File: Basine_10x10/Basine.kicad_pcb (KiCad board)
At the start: 2 copper layers, 100 x 100 mm, 55 parts, among them J1 2060-451/998-404, J10 2060-451/998-404, J11 2060-451/998-404, J12 2060-451/998-404, J13 2060-451/998-404, J14 2060-451/998-404, J15 2060-451/998-404, J16 2060-451/998-404, J17 2060-451/998-404, J18 2060-451/998-404, J2 2060-451/998-404, J3 2060-451/998-404, J4 2060-451/998-404, J5 2060-451/998-404, J6 2060-451/998-404, J7 2060-451/998-404, J8 2060-451/998-404, J9 2060-451/998-404

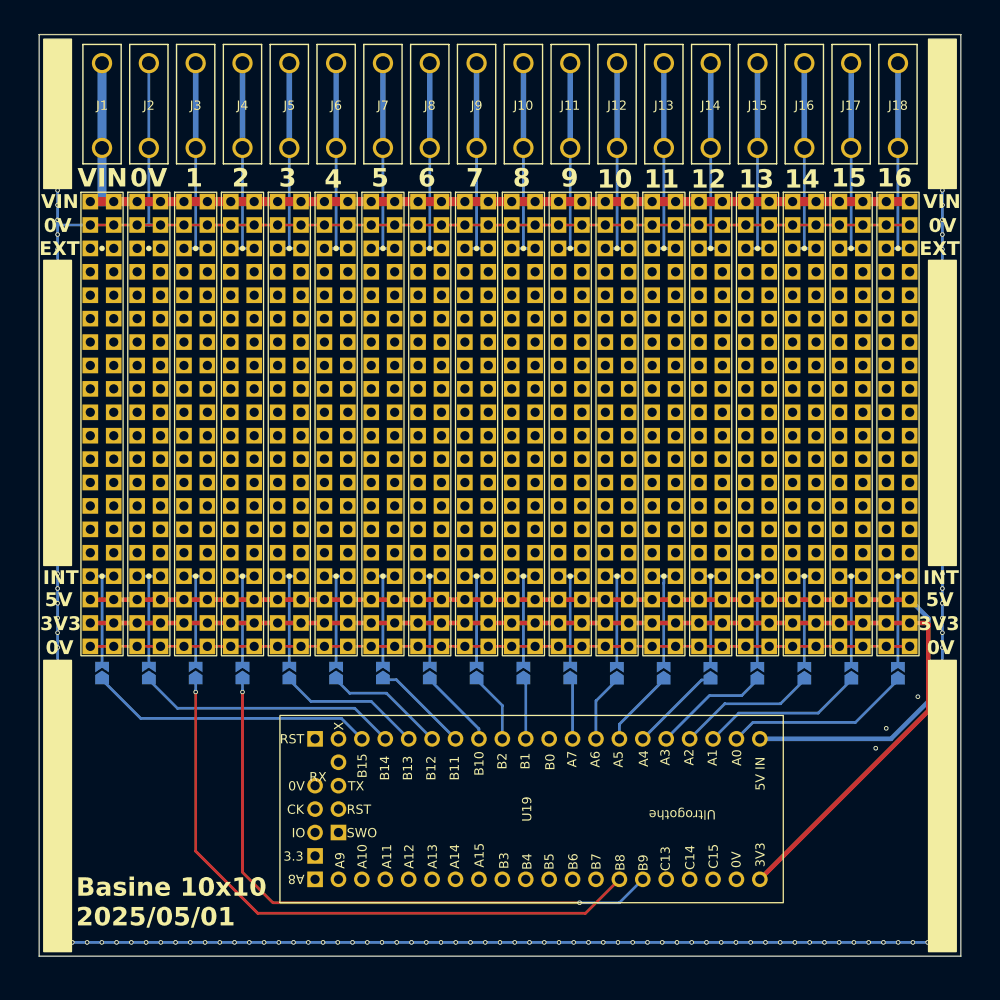
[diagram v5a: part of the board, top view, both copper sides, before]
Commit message: Basine_10x10 : moins de vias
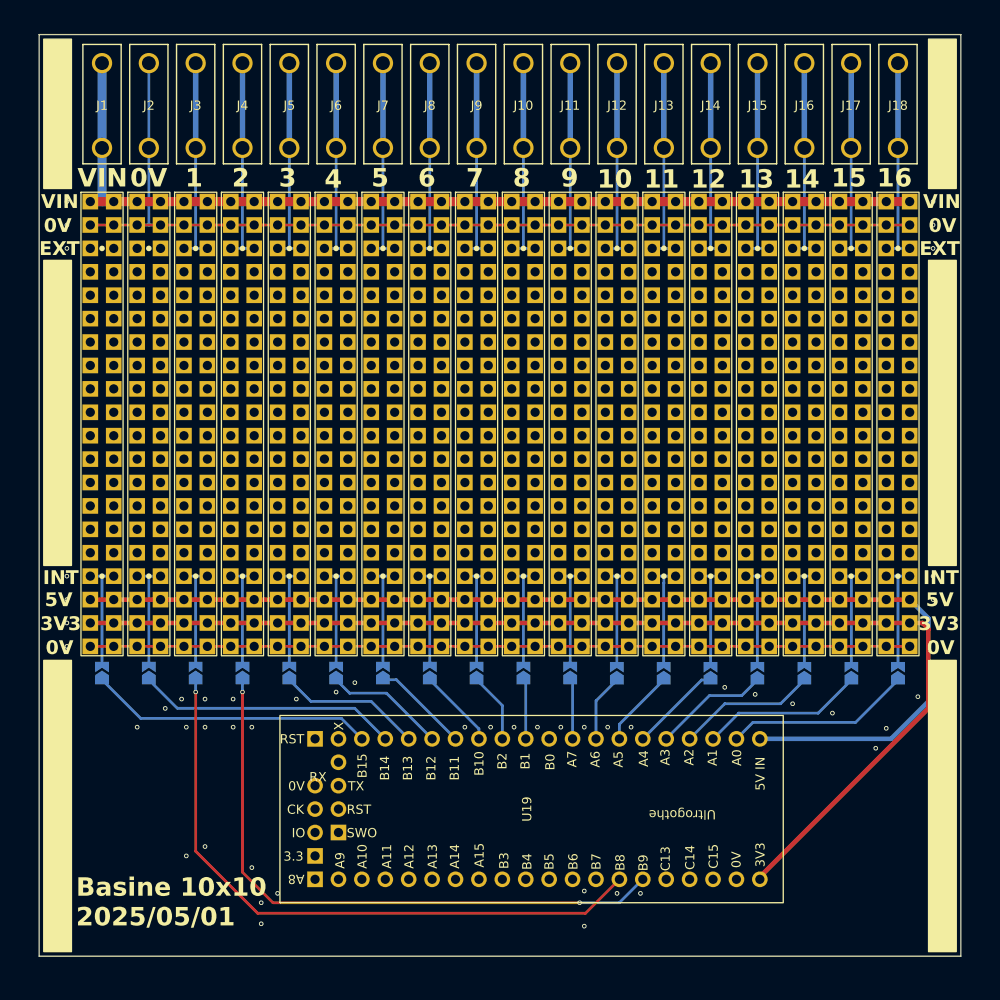
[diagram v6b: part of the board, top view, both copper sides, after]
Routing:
- net 0V: track 489.5 -> 197.9 mm, vias 184 -> 109

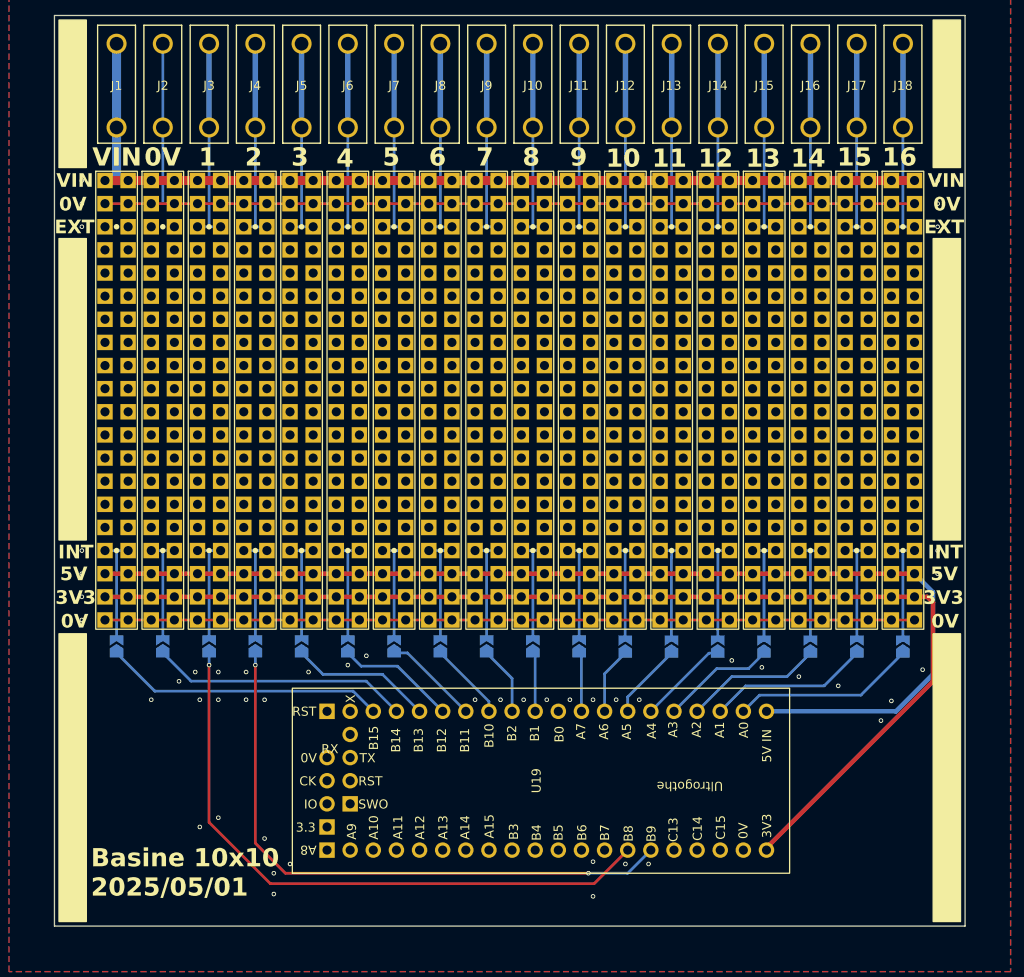
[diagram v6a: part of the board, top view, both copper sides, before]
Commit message: Basine 10x10: modification ultrogothe, allumettes, 3v3 en option
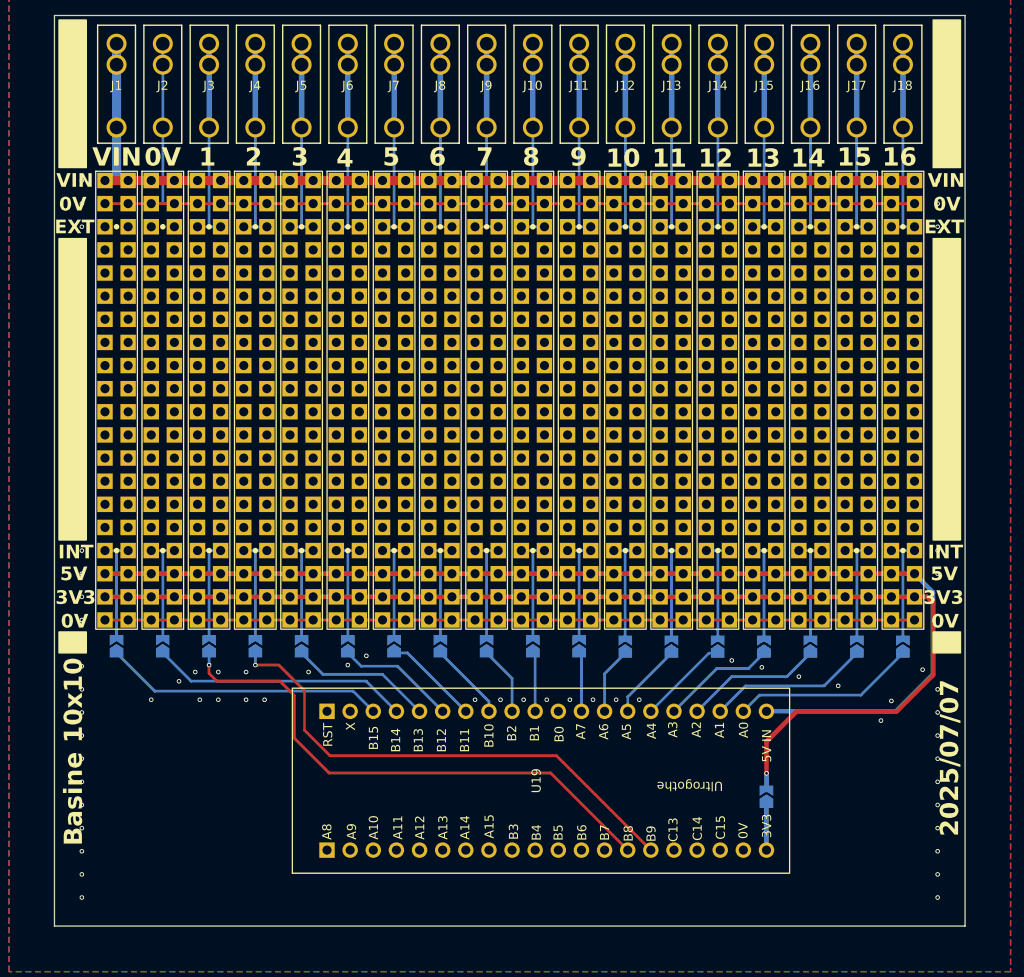
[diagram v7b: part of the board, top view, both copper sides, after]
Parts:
- added JP19: SolderJumper_2_Open, Jumper:SolderJumper-2_P1.3mm_Open_TrianglePad1.0x1.5mm, B.Cu at (178.2, 185.8)
- J1, J10, J11, J12, J13, J14, J15, J16, J17, J18, J2, J3, J4, J5, J6, J7, J8, J9: footprint Chimere_comps:CONN_2060-1451_998-404_WAGO -> Chimere_comps:Conn_bornier_et_wago
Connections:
- U1 pad 10: (no net) -> unconnected-(U1-Pad10)
- U1 pad 11: (no net) -> unconnected-(U1-Pad11)
- U1 pad 12: (no net) -> unconnected-(U1-Pad12)
- U1 pad 13: (no net) -> unconnected-(U1-Pad13)_1
- U1 pad 14: (no net) -> unconnected-(U1-Pad14)
- U1 pad 15: (no net) -> unconnected-(U1-Pad15)
- U1 pad 16: (no net) -> unconnected-(U1-Pad16)
- U1 pad 17: (no net) -> unconnected-(U1-Pad17)
- U1 pad 5: (no net) -> unconnected-(U1-Pad5)
- U1 pad 6: (no net) -> unconnected-(U1-Pad6)
- U1 pad 7: (no net) -> unconnected-(U1-Pad7)_1
- U1 pad 8: (no net) -> unconnected-(U1-Pad8)_1
- U1 pad 9: (no net) -> unconnected-(U1-Pad9)
- U10 pad 10: (no net) -> unconnected-(U10-Pad10)
- U10 pad 11: (no net) -> unconnected-(U10-Pad11)
- U10 pad 12: (no net) -> unconnected-(U10-Pad12)_1
- U10 pad 13: (no net) -> unconnected-(U10-Pad13)
- U10 pad 14: (no net) -> unconnected-(U10-Pad14)_1
- U10 pad 15: (no net) -> unconnected-(U10-Pad15)
- U10 pad 16: (no net) -> unconnected-(U10-Pad16)
- U10 pad 17: (no net) -> unconnected-(U10-Pad17)_1
- U10 pad 5: (no net) -> unconnected-(U10-Pad5)_1
- U10 pad 6: (no net) -> unconnected-(U10-Pad6)
- U10 pad 7: (no net) -> unconnected-(U10-Pad7)
- U10 pad 8: (no net) -> unconnected-(U10-Pad8)
- U10 pad 9: (no net) -> unconnected-(U10-Pad9)
- U11 pad 10: (no net) -> unconnected-(U11-Pad10)
- U11 pad 11: (no net) -> unconnected-(U11-Pad11)
- U11 pad 12: (no net) -> unconnected-(U11-Pad12)_1
- U11 pad 13: (no net) -> unconnected-(U11-Pad13)_1
- U11 pad 14: (no net) -> unconnected-(U11-Pad14)_1
- U11 pad 15: (no net) -> unconnected-(U11-Pad15)
- U11 pad 16: (no net) -> unconnected-(U11-Pad16)_1
- U11 pad 17: (no net) -> unconnected-(U11-Pad17)_1
- U11 pad 5: (no net) -> unconnected-(U11-Pad5)_1
- U11 pad 6: (no net) -> unconnected-(U11-Pad6)
- U11 pad 7: (no net) -> unconnected-(U11-Pad7)
- U11 pad 8: (no net) -> unconnected-(U11-Pad8)_1
- U11 pad 9: (no net) -> unconnected-(U11-Pad9)
- U12 pad 10: (no net) -> unconnected-(U12-Pad10)_1
- U12 pad 11: (no net) -> unconnected-(U12-Pad11)_1
- U12 pad 12: (no net) -> unconnected-(U12-Pad12)
- U12 pad 13: (no net) -> unconnected-(U12-Pad13)_1
- U12 pad 14: (no net) -> unconnected-(U12-Pad14)
- U12 pad 15: (no net) -> unconnected-(U12-Pad15)_1
- U12 pad 16: (no net) -> unconnected-(U12-Pad16)
- U12 pad 17: (no net) -> unconnected-(U12-Pad17)_1
- U12 pad 5: (no net) -> unconnected-(U12-Pad5)_1
- U12 pad 6: (no net) -> unconnected-(U12-Pad6)_1
- U12 pad 7: (no net) -> unconnected-(U12-Pad7)
- U12 pad 8: (no net) -> unconnected-(U12-Pad8)
- U12 pad 9: (no net) -> unconnected-(U12-Pad9)_1
- U13 pad 10: (no net) -> unconnected-(U13-Pad10)
- U13 pad 11: (no net) -> unconnected-(U13-Pad11)
- U13 pad 12: (no net) -> unconnected-(U13-Pad12)
- U13 pad 13: (no net) -> unconnected-(U13-Pad13)
- U13 pad 14: (no net) -> unconnected-(U13-Pad14)
- U13 pad 15: (no net) -> unconnected-(U13-Pad15)_1
- U13 pad 16: (no net) -> unconnected-(U13-Pad16)
- U13 pad 17: (no net) -> unconnected-(U13-Pad17)_1
- U13 pad 5: (no net) -> unconnected-(U13-Pad5)_1
- U13 pad 6: (no net) -> unconnected-(U13-Pad6)
- U13 pad 7: (no net) -> unconnected-(U13-Pad7)_1
- U13 pad 8: (no net) -> unconnected-(U13-Pad8)
- U13 pad 9: (no net) -> unconnected-(U13-Pad9)_1
- U14 pad 10: (no net) -> unconnected-(U14-Pad10)
- U14 pad 11: (no net) -> unconnected-(U14-Pad11)
- U14 pad 12: (no net) -> unconnected-(U14-Pad12)
- U14 pad 13: (no net) -> unconnected-(U14-Pad13)_1
- U14 pad 14: (no net) -> unconnected-(U14-Pad14)_1
- U14 pad 15: (no net) -> unconnected-(U14-Pad15)
- U14 pad 16: (no net) -> unconnected-(U14-Pad16)_1
- U14 pad 17: (no net) -> unconnected-(U14-Pad17)
- U14 pad 5: (no net) -> unconnected-(U14-Pad5)
- U14 pad 6: (no net) -> unconnected-(U14-Pad6)_1
- U14 pad 7: (no net) -> unconnected-(U14-Pad7)
- U14 pad 8: (no net) -> unconnected-(U14-Pad8)
- U14 pad 9: (no net) -> unconnected-(U14-Pad9)_1
- U15 pad 10: (no net) -> unconnected-(U15-Pad10)_1
- U15 pad 11: (no net) -> unconnected-(U15-Pad11)_1
- U15 pad 12: (no net) -> unconnected-(U15-Pad12)
- U15 pad 13: (no net) -> unconnected-(U15-Pad13)_1
- U15 pad 14: (no net) -> unconnected-(U15-Pad14)
- U15 pad 15: (no net) -> unconnected-(U15-Pad15)
- U15 pad 16: (no net) -> unconnected-(U15-Pad16)
- U15 pad 17: (no net) -> unconnected-(U15-Pad17)_1
- U15 pad 5: (no net) -> unconnected-(U15-Pad5)_1
- U15 pad 6: (no net) -> unconnected-(U15-Pad6)_1
- U15 pad 7: (no net) -> unconnected-(U15-Pad7)
- U15 pad 8: (no net) -> unconnected-(U15-Pad8)_1
- U15 pad 9: (no net) -> unconnected-(U15-Pad9)_1
- U16 pad 10: (no net) -> unconnected-(U16-Pad10)_1
- U16 pad 11: (no net) -> unconnected-(U16-Pad11)_1
- U16 pad 12: (no net) -> unconnected-(U16-Pad12)
- U16 pad 13: (no net) -> unconnected-(U16-Pad13)
- U16 pad 14: (no net) -> unconnected-(U16-Pad14)
- U16 pad 15: (no net) -> unconnected-(U16-Pad15)_1
- U16 pad 16: (no net) -> unconnected-(U16-Pad16)
- U16 pad 17: (no net) -> unconnected-(U16-Pad17)
- U16 pad 5: (no net) -> unconnected-(U16-Pad5)
- U16 pad 6: (no net) -> unconnected-(U16-Pad6)
- U16 pad 7: (no net) -> unconnected-(U16-Pad7)
- U16 pad 8: (no net) -> unconnected-(U16-Pad8)_1
- U16 pad 9: (no net) -> unconnected-(U16-Pad9)_1
- U17 pad 10: (no net) -> unconnected-(U17-Pad10)_1
- U17 pad 11: (no net) -> unconnected-(U17-Pad11)_1
- U17 pad 12: (no net) -> unconnected-(U17-Pad12)_1
- U17 pad 13: (no net) -> unconnected-(U17-Pad13)
- U17 pad 14: (no net) -> unconnected-(U17-Pad14)_1
- U17 pad 15: (no net) -> unconnected-(U17-Pad15)_1
- U17 pad 16: (no net) -> unconnected-(U17-Pad16)
- U17 pad 17: (no net) -> unconnected-(U17-Pad17)_1
- U17 pad 5: (no net) -> unconnected-(U17-Pad5)
- U17 pad 6: (no net) -> unconnected-(U17-Pad6)_1
- U17 pad 7: (no net) -> unconnected-(U17-Pad7)_1
- U17 pad 8: (no net) -> unconnected-(U17-Pad8)
- U17 pad 9: (no net) -> unconnected-(U17-Pad9)_1
- U18 pad 10: (no net) -> unconnected-(U18-Pad10)
- U18 pad 11: (no net) -> unconnected-(U18-Pad11)
- U18 pad 12: (no net) -> unconnected-(U18-Pad12)_1
- U18 pad 13: (no net) -> unconnected-(U18-Pad13)
- U18 pad 14: (no net) -> unconnected-(U18-Pad14)_1
- U18 pad 15: (no net) -> unconnected-(U18-Pad15)
- U18 pad 16: (no net) -> unconnected-(U18-Pad16)_1
- U18 pad 17: (no net) -> unconnected-(U18-Pad17)
- U18 pad 5: (no net) -> unconnected-(U18-Pad5)
- U18 pad 6: (no net) -> unconnected-(U18-Pad6)_1
- U18 pad 7: (no net) -> unconnected-(U18-Pad7)_1
- U18 pad 8: (no net) -> unconnected-(U18-Pad8)_1
- U18 pad 9: (no net) -> unconnected-(U18-Pad9)_1
- U19 pad 20: 3V3 -> Net-(JP19-A)
- U2 pad 10: (no net) -> unconnected-(U2-Pad10)
- U2 pad 11: (no net) -> unconnected-(U2-Pad11)_1
- U2 pad 12: (no net) -> unconnected-(U2-Pad12)
- U2 pad 13: (no net) -> unconnected-(U2-Pad13)
- U2 pad 14: (no net) -> unconnected-(U2-Pad14)_1
- U2 pad 15: (no net) -> unconnected-(U2-Pad15)
- U2 pad 16: (no net) -> unconnected-(U2-Pad16)
- U2 pad 17: (no net) -> unconnected-(U2-Pad17)
- U2 pad 5: (no net) -> unconnected-(U2-Pad5)
- U2 pad 6: (no net) -> unconnected-(U2-Pad6)
- U2 pad 7: (no net) -> unconnected-(U2-Pad7)_1
- U2 pad 8: (no net) -> unconnected-(U2-Pad8)_1
- U2 pad 9: (no net) -> unconnected-(U2-Pad9)_1
- U3 pad 10: (no net) -> unconnected-(U3-Pad10)_1
- U3 pad 11: (no net) -> unconnected-(U3-Pad11)
- U3 pad 12: (no net) -> unconnected-(U3-Pad12)_1
- U3 pad 13: (no net) -> unconnected-(U3-Pad13)_1
- U3 pad 14: (no net) -> unconnected-(U3-Pad14)
- U3 pad 15: (no net) -> unconnected-(U3-Pad15)
- U3 pad 16: (no net) -> unconnected-(U3-Pad16)_1
- U3 pad 17: (no net) -> unconnected-(U3-Pad17)
- U3 pad 5: (no net) -> unconnected-(U3-Pad5)_1
- U3 pad 6: (no net) -> unconnected-(U3-Pad6)_1
- U3 pad 7: (no net) -> unconnected-(U3-Pad7)_1
- U3 pad 8: (no net) -> unconnected-(U3-Pad8)
- U3 pad 9: (no net) -> unconnected-(U3-Pad9)_1
- U4 pad 10: (no net) -> unconnected-(U4-Pad10)
- U4 pad 11: (no net) -> unconnected-(U4-Pad11)
- U4 pad 12: (no net) -> unconnected-(U4-Pad12)_1
- U4 pad 13: (no net) -> unconnected-(U4-Pad13)
- U4 pad 14: (no net) -> unconnected-(U4-Pad14)_1
- U4 pad 15: (no net) -> unconnected-(U4-Pad15)_1
- U4 pad 16: (no net) -> unconnected-(U4-Pad16)_1
- U4 pad 17: (no net) -> unconnected-(U4-Pad17)
- U4 pad 5: (no net) -> unconnected-(U4-Pad5)_1
- U4 pad 6: (no net) -> unconnected-(U4-Pad6)_1
- U4 pad 7: (no net) -> unconnected-(U4-Pad7)
- U4 pad 8: (no net) -> unconnected-(U4-Pad8)_1
- U4 pad 9: (no net) -> unconnected-(U4-Pad9)_1
- U5 pad 10: (no net) -> unconnected-(U5-Pad10)_1
- U5 pad 11: (no net) -> unconnected-(U5-Pad11)
- U5 pad 12: (no net) -> unconnected-(U5-Pad12)
- U5 pad 13: (no net) -> unconnected-(U5-Pad13)_1
- U5 pad 14: (no net) -> unconnected-(U5-Pad14)_1
- U5 pad 15: (no net) -> unconnected-(U5-Pad15)_1
- U5 pad 16: (no net) -> unconnected-(U5-Pad16)_1
- U5 pad 17: (no net) -> unconnected-(U5-Pad17)
- U5 pad 5: (no net) -> unconnected-(U5-Pad5)_1
- U5 pad 6: (no net) -> unconnected-(U5-Pad6)
- U5 pad 7: (no net) -> unconnected-(U5-Pad7)_1
- U5 pad 8: (no net) -> unconnected-(U5-Pad8)
- U5 pad 9: (no net) -> unconnected-(U5-Pad9)
- U6 pad 10: (no net) -> unconnected-(U6-Pad10)_1
- U6 pad 11: (no net) -> unconnected-(U6-Pad11)_1
- U6 pad 12: (no net) -> unconnected-(U6-Pad12)
- U6 pad 13: (no net) -> unconnected-(U6-Pad13)_1
- U6 pad 14: (no net) -> unconnected-(U6-Pad14)_1
- U6 pad 15: (no net) -> unconnected-(U6-Pad15)
- U6 pad 16: (no net) -> unconnected-(U6-Pad16)_1
- U6 pad 17: (no net) -> unconnected-(U6-Pad17)_1
- U6 pad 5: (no net) -> unconnected-(U6-Pad5)_1
- U6 pad 6: (no net) -> unconnected-(U6-Pad6)_1
- U6 pad 7: (no net) -> unconnected-(U6-Pad7)_1
- U6 pad 8: (no net) -> unconnected-(U6-Pad8)_1
- U6 pad 9: (no net) -> unconnected-(U6-Pad9)_1
- U7 pad 10: (no net) -> unconnected-(U7-Pad10)
- U7 pad 11: (no net) -> unconnected-(U7-Pad11)_1
- U7 pad 12: (no net) -> unconnected-(U7-Pad12)_1
- U7 pad 13: (no net) -> unconnected-(U7-Pad13)
- U7 pad 14: (no net) -> unconnected-(U7-Pad14)
- U7 pad 15: (no net) -> unconnected-(U7-Pad15)
- U7 pad 16: (no net) -> unconnected-(U7-Pad16)_1
- U7 pad 17: (no net) -> unconnected-(U7-Pad17)
- U7 pad 5: (no net) -> unconnected-(U7-Pad5)
- U7 pad 6: (no net) -> unconnected-(U7-Pad6)_1
- U7 pad 7: (no net) -> unconnected-(U7-Pad7)_1
- U7 pad 8: (no net) -> unconnected-(U7-Pad8)_1
- U7 pad 9: (no net) -> unconnected-(U7-Pad9)_1
- U8 pad 10: (no net) -> unconnected-(U8-Pad10)_1
- U8 pad 11: (no net) -> unconnected-(U8-Pad11)
- U8 pad 12: (no net) -> unconnected-(U8-Pad12)_1
- U8 pad 13: (no net) -> unconnected-(U8-Pad13)_1
- U8 pad 14: (no net) -> unconnected-(U8-Pad14)
- U8 pad 15: (no net) -> unconnected-(U8-Pad15)
- U8 pad 16: (no net) -> unconnected-(U8-Pad16)_1
- U8 pad 17: (no net) -> unconnected-(U8-Pad17)_1
- U8 pad 5: (no net) -> unconnected-(U8-Pad5)
- U8 pad 6: (no net) -> unconnected-(U8-Pad6)_1
- U8 pad 7: (no net) -> unconnected-(U8-Pad7)
- U8 pad 8: (no net) -> unconnected-(U8-Pad8)
- U8 pad 9: (no net) -> unconnected-(U8-Pad9)_1
- U9 pad 10: (no net) -> unconnected-(U9-Pad10)_1
- U9 pad 11: (no net) -> unconnected-(U9-Pad11)_1
- U9 pad 12: (no net) -> unconnected-(U9-Pad12)_1
- U9 pad 13: (no net) -> unconnected-(U9-Pad13)
- U9 pad 14: (no net) -> unconnected-(U9-Pad14)
- U9 pad 15: (no net) -> unconnected-(U9-Pad15)
- U9 pad 16: (no net) -> unconnected-(U9-Pad16)
- U9 pad 17: (no net) -> unconnected-(U9-Pad17)_1
- U9 pad 5: (no net) -> unconnected-(U9-Pad5)
- U9 pad 6: (no net) -> unconnected-(U9-Pad6)
- U9 pad 7: (no net) -> unconnected-(U9-Pad7)
- U9 pad 8: (no net) -> unconnected-(U9-Pad8)
- U9 pad 9: (no net) -> unconnected-(U9-Pad9)_1
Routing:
- net CAN_TX: track 66.7 -> 55.7 mm, vias 2 -> 1
- net CAN_RX: track 68.9 -> 59.0 mm
- net Net-(JP19-A): track 0.00 -> 5.14 mm
- net 3V3: track 125.9 -> 125.8 mm, vias 0 -> 1
- net 0V: vias 109 -> 99
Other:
- board text added: "2025/07/07"
- board text added: "Basine 10x10"
- board text removed: "Basine 10x10 2025/05/01"
